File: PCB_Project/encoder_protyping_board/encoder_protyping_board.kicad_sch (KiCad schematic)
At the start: 11 parts, among them J1 Conn_02x04_Counter_Clockwise, J2 Conn_01x02_Pin, J3 Conn_01x03_Pin

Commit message: the filter cap does not go between the voltage rail and the input pin
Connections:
- net +12V: now also C3.1, U2.3 (VBB); no longer C3.2
- net GND: now also C3.2
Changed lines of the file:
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@@
   (junction (at 76.2 90.17) (diameter 0) (color 0 0 0 0)
+  )
+  (junction (at 148.59 80.01) (diameter 0) (color 0 0 0 0)
   )
   (no_connect (at 115.57 77.47))
@@
     )
   )
+  (global_label "GND" (shape input) (at 148.59 72.39 90) (fields_autoplaced)
+    (effects (font (size 1.27 1.27)) (justify left))
+    (property "Intersheetrefs" "${INTERSHEET_REFS}" (at 148.59 65.5343 90)
+      (effects (font (size 1.27 1.27)) (justify left) hide)
+    )
+  )
   (global_label "GND" (shape input) (at 92.71 92.71 180) (fields_autoplaced)
     (effects (font (size 1.27 1.27)) (justify right))
@@
     )
   )
-  (symbol (lib_id "power:+12V") (at 148.59 72.39 0) (unit 1)
-    (in_bom yes) (on_board yes) (dnp no) (fields_autoplaced)
-    (property "Reference" "#PWR03" (at 148.59 76.2 0)
-      (effects (font (size 1.27 1.27)) hide)
-    )
-    (property "Value" "+12V" (at 148.59 67.31 0)
-      (effects (font (size 1.27 1.27)))
-    )
-    (property "Footprint" "" (at 148.59 72.39 0)
-      (effects (font (size 1.27 1.27)) hide)
-    )
-    (property "Datasheet" "" (at 148.59 72.39 0)
-      (effects (font (size 1.27 1.27)) hide)
-    )
-    (pin "1")
-    (instances
-      (project "encoder_protyping_board"
-        (path "/216c1417-8a2a-4718-9426-b99cd58fdcbb"
-          (reference "#PWR03") (unit 1)
-        )
-      )
-    )
-  )
   (symbol (lib_id "Device:C") (at 69.85 93.98 0) (unit 1)
     (in_bom yes) (on_board yes) (dnp no) (fields_autoplaced)
@@
         )
       )
+    )
+  )
+  (symbol (lib_id "power:+12V") (at 148.59 80.01 90) (unit 1)
+    (in_bom yes) (on_board yes) (dnp no) (fields_autoplaced)
+    (property "Reference" "#PWR09" (at 152.4 80.01 0)
+      (effects (font (size 1.27 1.27)) hide)
+    )
+    (property "Value" "+12V" (at 144.78 80.01 90)
+      (effects (font (size 1.27 1.27)) (justify left))
+    )
+    (property "Footprint" "" (at 148.59 80.01 0)
+      (effects (font (size 1.27 1.27)) hide)
+    )
+    (property "Datasheet" "" (at 148.59 80.01 0)
+      (effects (font (size 1.27 1.27)) hide)
+    )
+    (pin "1")
+    (instances
+      (project "encoder_protyping_board"
+        (path "/216c1417-8a2a-4718-9426-b99cd58fdcbb"
+          (reference "#PWR09") (unit 1)
+        )
+      )

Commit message: I have probably done so many things wrong
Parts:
- C1, C2: footprint (none) -> Capacitor_SMD:C_0402_1005Metric
- C3: footprint (none) -> Capacitor_THT:CP_Radial_D5.0mm_P2.00mm
- R1, R2, R3: footprint (none) -> Resistor_SMD:R_0402_1005Metric
- U2: footprint (none) -> Package_SO:SSOP-10_3.9x4.9mm_P1.00mm
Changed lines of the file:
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@@
       (effects (font (size 1.27 1.27)) (justify right))
     )
-    (property "Footprint" "" (at 44.958 62.23 90)
+    (property "Footprint" "Resistor_SMD:R_0402_1005Metric" (at 44.958 62.23 90)
       (effects (font (size 1.27 1.27)) hide)
     )
@@
       (effects (font (size 1.27 1.27)) (justify left))
     )
-    (property "Footprint" "" (at 147.6248 72.39 0)
+    (property "Footprint" "Capacitor_THT:CP_Radial_D5.0mm_P2.00mm" (at 147.6248 72.39 0)
       (effects (font (size 1.27 1.27)) hide)
     )
@@
       (effects (font (size 1.27 1.27)) (justify left))
     )
-    (property "Footprint" "" (at 77.1652 97.79 0)
+    (property "Footprint" "Capacitor_SMD:C_0402_1005Metric" (at 77.1652 97.79 0)
       (effects (font (size 1.27 1.27)) hide)
     )
@@
       (effects (font (size 1.27 1.27)) (justify right))
     )
-    (property "Footprint" "" (at 70.8152 97.79 0)
+    (property "Footprint" "Capacitor_SMD:C_0402_1005Metric" (at 70.8152 97.79 0)
       (effects (font (size 1.27 1.27)) hide)
     )
@@
       (effects (font (size 1.27 1.27)))
     )
-    (property "Footprint" "" (at 157.48 92.71 0)
-      (effects (font (size 1.27 1.27)) hide)
+    (property "Footprint" "Package_SO:SSOP-10_3.9x4.9mm_P1.00mm" (at 157.48 92.71 0)
+      (effects (font (size 1.27 1.27)))
     )
     (property "Datasheet" "" (at 157.48 92.71 0)
@@
       (effects (font (size 1.27 1.27)) (justify right))
     )
-    (property "Footprint" "" (at 44.958 72.39 90)
+    (property "Footprint" "Resistor_SMD:R_0402_1005Metric" (at 44.958 72.39 90)
       (effects (font (size 1.27 1.27)) hide)
     )
@@
       (effects (font (size 1.27 1.27)))
     )
-    (property "Footprint" "" (at 88.9 77.978 90)
-      (effects (font (size 1.27 1.27)) hide)
-    )
+    (property "Footprint" "Resistor_SMD:R_0402_1005Metric" (at 88.9 77.978 90)
+      (effects (font (size 1.27 1.27)) hide)
+    )

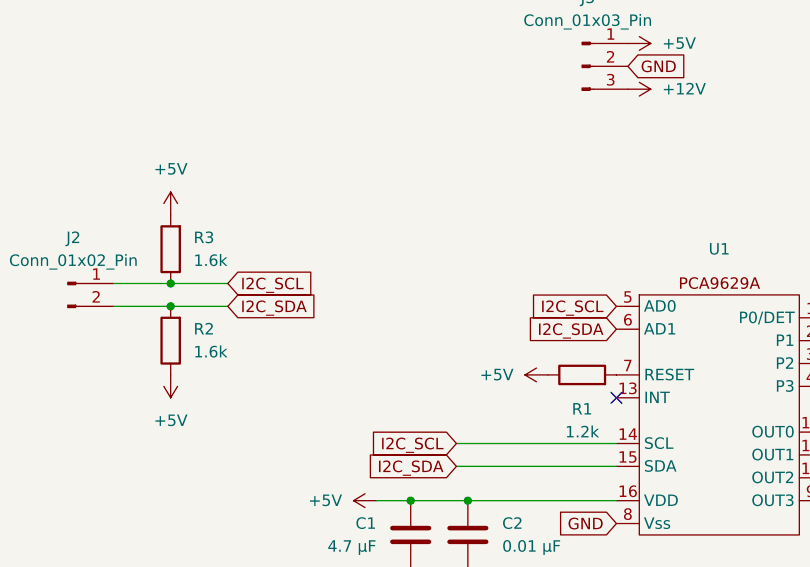
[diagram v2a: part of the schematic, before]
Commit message: added addresse jumpers
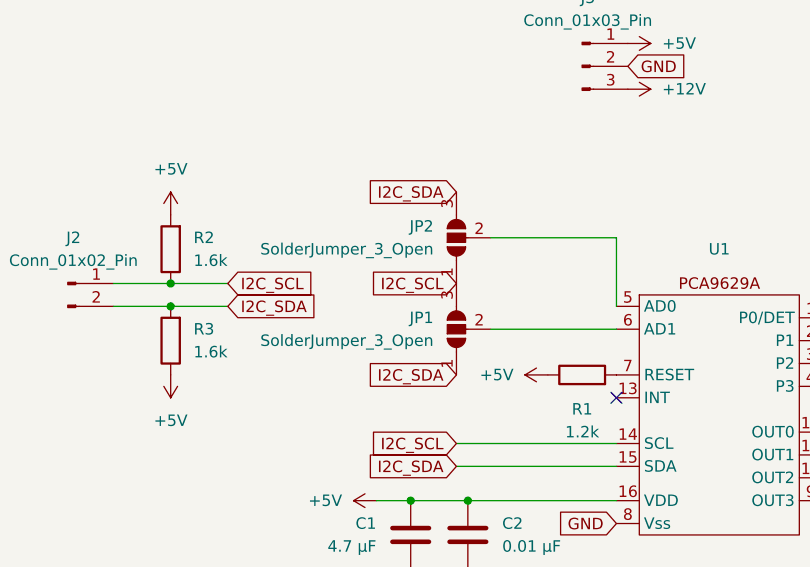
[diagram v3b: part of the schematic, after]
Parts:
- added JP1: SolderJumper_3_Open, Jumper:SolderJumper-3_P1.3mm_Open_RoundedPad1.0x1.5mm, symbol Jumper:SolderJumper_3_Open
- added JP2: SolderJumper_3_Open, Jumper:SolderJumper-3_P1.3mm_Open_RoundedPad1.0x1.5mm_NumberLabels, symbol Jumper:SolderJumper_3_Open
- renumbered R3 to R2, R2 to R3
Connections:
- net I2C_SCL: now also JP1.3 (B), JP2.1 (A); no longer U1.5 (AD0)
- net I2C_SDA: now also JP1.1 (A), JP2.3 (B); no longer U1.6 (AD1)
- new net: JP2.2 (C), U1.5 (AD0)
- new net: JP1.2 (C), U1.6 (AD1)
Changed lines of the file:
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@@
   (no_connect (at 92.71 78.74))
   (no_connect (at 115.57 74.93))
+  (wire (pts (xy 92.71 60.96) (xy 92.71 68.58))
+    (stroke (width 0) (type default))
+  )
+  (wire (pts (xy 78.74 60.96) (xy 92.71 60.96))
+    (stroke (width 0) (type default))
+  )
   (wire (pts (xy 115.57 85.09) (xy 148.59 85.09))
     (stroke (width 0) (type default))
@@
   )
   (wire (pts (xy 115.57 72.39) (xy 144.78 72.39))
+    (stroke (width 0) (type default))
+  )
+  (wire (pts (xy 78.74 71.12) (xy 92.71 71.12))
     (stroke (width 0) (type default))
   )
@@
     )
   )
-  (global_label "I2C_SCL" (shape input) (at 92.71 68.58 180) (fields_autoplaced)
-    (effects (font (size 1.27 1.27)) (justify right))
-    (property "Intersheetrefs" "${INTERSHEET_REFS}" (at 82.1653 68.58 0)
-      (effects (font (size 1.27 1.27)) (justify right) hide)
-    )
-  )
   (global_label "I2C_SDA" (shape input) (at 49.53 68.58 0) (fields_autoplaced)
     (effects (font (size 1.27 1.27)) (justify left))
@@
     )
   )
-  (global_label "I2C_SDA" (shape input) (at 92.71 71.12 180) (fields_autoplaced)
-    (effects (font (size 1.27 1.27)) (justify right))
-    (property "Intersheetrefs" "${INTERSHEET_REFS}" (at 82.1048 71.12 0)
+  (global_label "I2C_SDA" (shape input) (at 74.93 55.88 180) (fields_autoplaced)
+    (effects (font (size 1.27 1.27)) (justify right))
+    (property "Intersheetrefs" "${INTERSHEET_REFS}" (at 64.3248 55.88 0)
       (effects (font (size 1.27 1.27)) (justify right) hide)
     )
@@
     )
   )
+  (global_label "I2C_SCL" (shape input) (at 74.93 66.04 180) (fields_autoplaced)
+    (effects (font (size 1.27 1.27)) (justify right))
+    (property "Intersheetrefs" "${INTERSHEET_REFS}" (at 64.3853 66.04 0)
+      (effects (font (size 1.27 1.27)) (justify right) hide)
+    )
+  )
   (global_label "GND" (shape input) (at 93.98 41.91 0) (fields_autoplaced)
     (effects (font (size 1.27 1.27)) (justify left))
@@
     )
   )
+  (global_label "I2C_SDA" (shape input) (at 74.93 76.2 180) (fields_autoplaced)
+    (effects (font (size 1.27 1.27)) (justify right))
+    (property "Intersheetrefs" "${INTERSHEET_REFS}" (at 64.3248 76.2 0)
+      (effects (font (size 1.27 1.27)) (justify right) hide)
+    )
+  )
   (symbol (lib_id "Device:R") (at 43.18 62.23 180) (unit 1)
     (in_bom yes) (on_board yes) (dnp no) (fields_autoplaced)
-    (property "Reference" "R3" (at 45.72 60.96 0)
+    (property "Reference" "R2" (at 45.72 60.96 0)
       (effects (font (size 1.27 1.27)) (justify right))
     )
@@
       (project "encoder_protyping_board"
         (path "/216c1417-8a2a-4718-9426-b99cd58fdcbb"
-          (reference "R3") (unit 1)
+          (reference "R2") (unit 1)
+        )
+      )
+    )
+  )
+  (symbol (lib_id "Jumper:SolderJumper_3_Open") (at 74.93 60.96 90) (unit 1)
+    (in_bom yes) (on_board yes) (dnp no) (fields_autoplaced)
+    (property "Reference" "JP2" (at 72.39 59.69 90)
+      (effects (font (size 1.27 1.27)) (justify left))
+    )
+    (property "Value" "SolderJumper_3_Open" (at 72.39 62.23 90)
+      (effects (font (size 1.27 1.27)) (justify left))
+    )
+    (property "Footprint" "Jumper:SolderJumper-3_P1.3mm_Open_RoundedPad1.0x1.5mm_NumberLabels" (at 74.93 60.96 0)
+      (effects (font (size 1.27 1.27)) hide)
+    )
+    (property "Datasheet" "~" (at 74.93 60.96 0)
+      (effects (font (size 1.27 1.27)) hide)
+    )
+    (pin "2")
+    (pin "1")
+    (pin "3")
+    (instances
+      (project "encoder_protyping_board"
+        (path "/216c1417-8a2a-4718-9426-b99cd58fdcbb"
+          (reference "JP2") (unit 1)
         )
       )
@@
         (path "/216c1417-8a2a-4718-9426-b99cd58fdcbb"
           (reference "#PWR05") (unit 1)
+        )
+      )
+    )
+  )
+  (symbol (lib_id "Jumper:SolderJumper_3_Open") (at 74.93 71.12 90) (unit 1)
+    (in_bom yes) (on_board yes) (dnp no) (fields_autoplaced)
+    (property "Reference" "JP1" (at 72.39 69.85 90)
+      (effects (font (size 1.27 1.27)) (justify left))
+    )
+    (property "Value" "SolderJumper_3_Open" (at 72.39 72.39 90)
+      (effects (font (size 1.27 1.27)) (justify left))
+    )
+    (property "Footprint" "Jumper:SolderJumper-3_P1.3mm_Open_RoundedPad1.0x1.5mm" (at 74.93 71.12 0)
+      (effects (font (size 1.27 1.27)) hide)
+    )
+    (property "Datasheet" "~" (at 74.93 71.12 0)
+      (effects (font (size 1.27 1.27)) hide)
+    )
+    (pin "2")
+    (pin "1")
+    (pin "3")
+    (instances
+      (project "encoder_protyping_board"
+        (path "/216c1417-8a2a-4718-9426-b99cd58fdcbb"
+          (reference "JP1") (unit 1)
         )
       )
@@
   (symbol (lib_id "Device:R") (at 43.18 72.39 180) (unit 1)
     (in_bom yes) (on_board yes) (dnp no) (fields_autoplaced)
-    (property "Reference" "R2" (at 45.72 71.12 0)
+    (property "Reference" "R3" (at 45.72 71.12 0)
       (effects (font (size 1.27 1.27)) (justify right))
     )
@@
       (project "encoder_protyping_board"
         (path "/216c1417-8a2a-4718-9426-b99cd58fdcbb"
-          (reference "R2") (unit 1)
-        )
-      )
+          (reference "R3") (unit 1)
+        )
+      )
